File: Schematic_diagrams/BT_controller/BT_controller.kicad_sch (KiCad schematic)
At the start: 41 parts, among them J1 Conn_01x02_Socket, J1 Conn_2_Pin, J10 Conn_01x15_Socket, J11 Screw_Terminal_13-24_double_r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, J12 Screw_Terminal_58-60_double_r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, J13 Screw_Terminal_61-72_double_r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, J15 Conn_7_Pin, J16 Conn_4_Pin, J17 Conn_4_Pin, J2 D Sub Conn_9_Pin, J3 D Sub Conn_15_Pin, J4 Conn_01x07_Socket, J5 Conn_01x07_Socket, J5 Conn_7_Pin, J6 Screw_Terminal_13-24_double_r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, J8 Screw_Terminal_37-41_double_r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, J9 Screw_Terminal_1-2_partial_do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, SW1 ON/OFF, SW1 Start, SW3 SW_SPDT

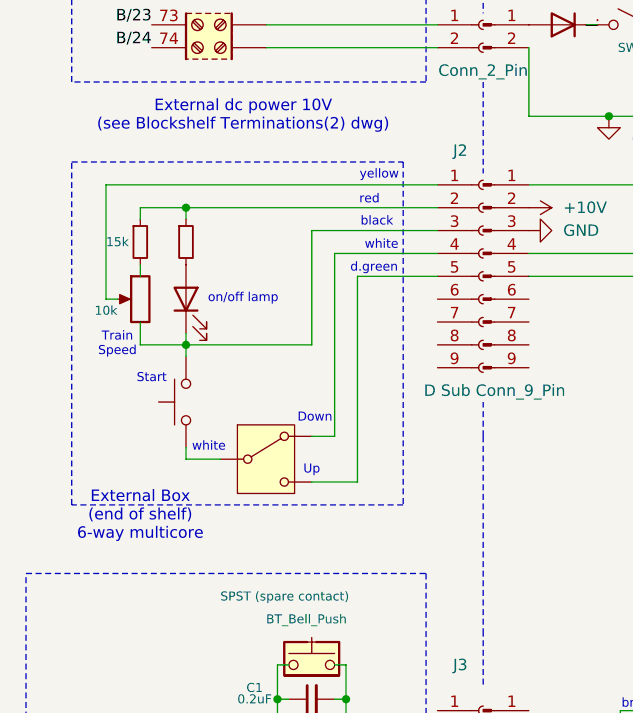
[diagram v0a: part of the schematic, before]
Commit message: control box update
addition of 1N4148 diodes to control box to enable the "start" button to apply to both the up and down lines
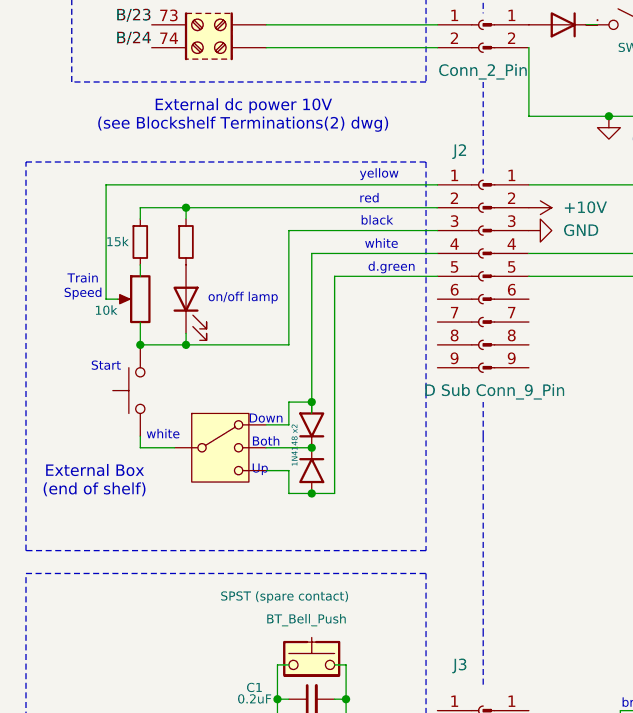
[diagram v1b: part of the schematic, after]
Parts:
- removed SW3: SW_SPDT, symbol Switch:SW_SPDT
- added D11: 1N4148 x2, Diode_SMD:D_MiniMELF, symbol Diode:LL4148
- added D12: 1N4148, Diode_SMD:D_MiniMELF, symbol Diode:LL4148
- added SW2: SW_SP3T, symbol Switch:SW_SP3T
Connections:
- net at SW1.1: now also SW2. (4)
- net at J4.4 (Pin_4): now also D12.2 (A), SW2. (4)
- net at J4.5 (Pin_5): now also D11.2 (A), SW2. (4)
- new net: D11.1 (K), D12.1 (K), SW2. (4)
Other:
- note added: "Both"
- note added: "External Box (end of shelf)"
- note removed: "External Box (end of shelf) 6-way multicore"

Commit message: zip files for controller
save zip files
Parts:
- added D13: 6x1N4148, Diode_THT:D_DO-35_SOD27_P7.62mm_Horizontal, symbol Diode:1N4148
- added D14, D15, D16, D17, D18: 1N4148, Diode_THT:D_DO-35_SOD27_P7.62mm_Horizontal, symbol Diode:1N4148
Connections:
- net at A2.20 (A1): now also D16.2 (A)
- net at A2.21 (A2): now also D17.2 (A)
- net at A2.22 (A3): now also D18.2 (A)
- net at A1.20 (A1): now also D13.2 (A)
- net at A1.21 (A2): now also D14.2 (A)
- net at A1.22 (A3): now also D15.2 (A)
- new net: D14.1 (K), D17.1 (K)
- new net: D15.1 (K), D18.1 (K)
- new net: D13.1 (K), D16.1 (K)
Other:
- note added: "flying lead grommet exit to AHB Control Box"

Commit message: Addition of AHB controller
Addition of AHB controller and modification of delays
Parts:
- added J14: Conn_01x05_Pin, symbol Connector:Conn_01x05_Pin
- added J3: Conn_5_pin, symbol Connector:Conn_01x05_Socket
- renumbered J3 to J4, J16 to J5, J4 to J6, J5 to J7
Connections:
- net +5V: now also J14.4 (Pin_4), J3.4 (Pin_4)
- net 0V: now also J3.5 (Pin_5)
- net GND: now also J14.5 (Pin_5)
- net <- Adversane: now reaches D14.1 (K), D17.1 (K)
- net <- Adversane: now also J14.2 (Pin_2)
- net <- Barns Green: now reaches D15.1 (K), D18.1 (K)
- net <- Barns Green: now also J14.3 (Pin_3)
- net <- Cray Lane: now reaches D13.1 (K), D16.1 (K)
- net <- Cray Lane: now also J14.1 (Pin_1)
- new net Adversane: J3.2 (Pin_2)
- new net Barns Green: J3.3 (Pin_3)
- new net Cray Lane: J3.1 (Pin_1)
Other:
- added sheet AHB Control Box (../AHB_control_box/AHB_control_box.kicad_sch)
- note added: "5-pin connector to AHB Control Box"
- note removed: "flying lead grommet exit to AHB Control Box"
